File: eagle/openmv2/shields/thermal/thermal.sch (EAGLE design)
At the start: 10 parts, among them U1 MLX90620, U3 2.6v

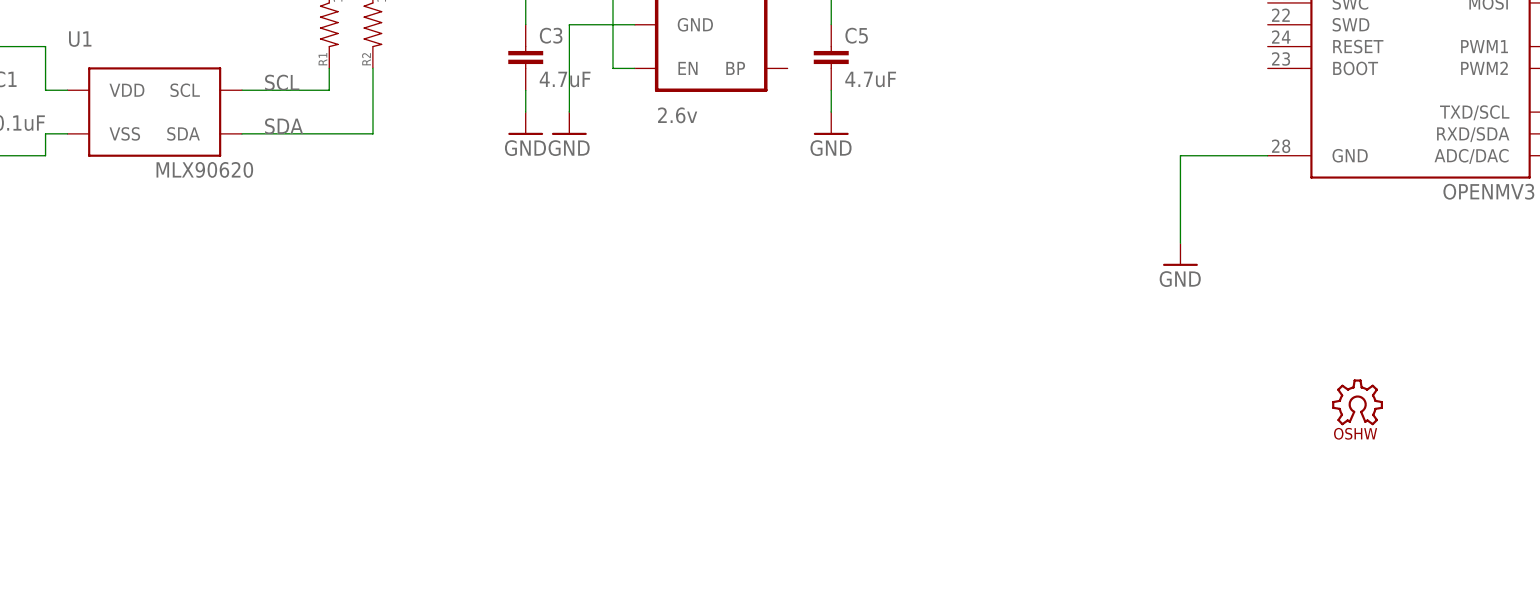
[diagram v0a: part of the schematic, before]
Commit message: Update shields silk-screen.
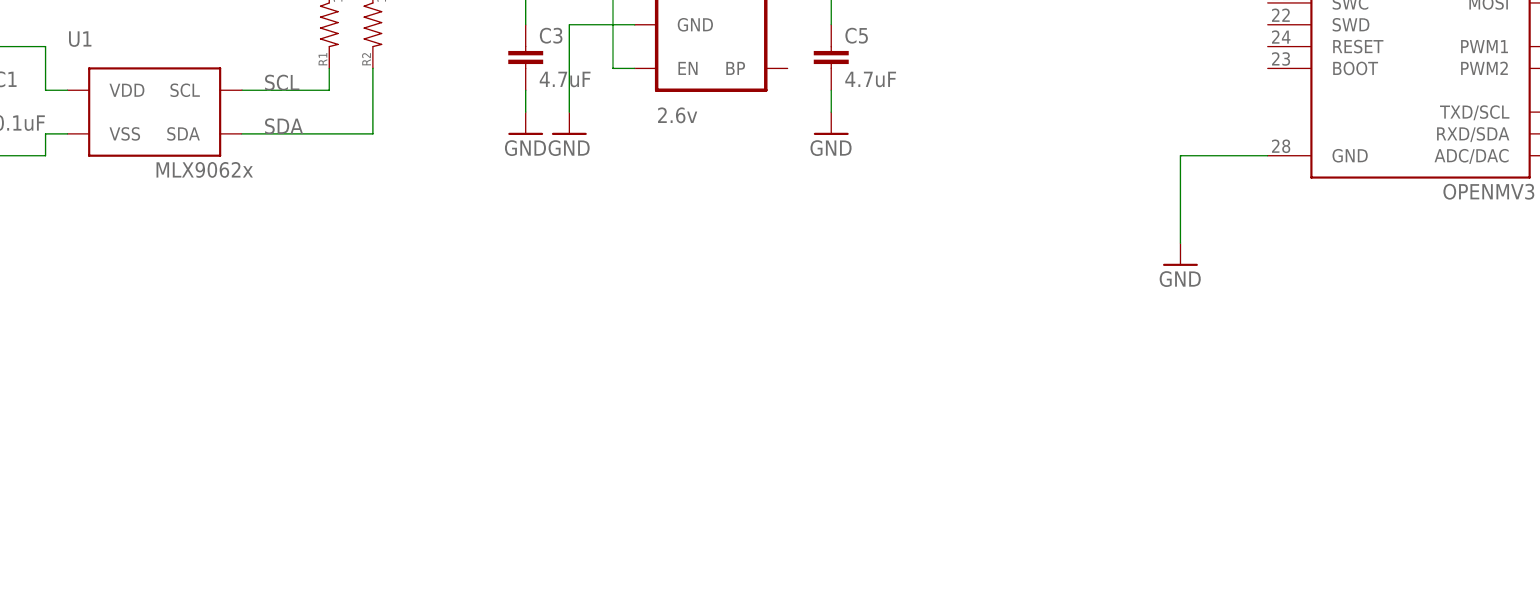
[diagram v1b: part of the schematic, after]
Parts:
- removed LOGO1: OSHW_LOGO_8MILX0150-NT, iofault:OSHW_LOGO_8MILX0150-NT
- U1: value MLX90620 -> MLX9062x
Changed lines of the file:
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@@
 <part name="GND4" library="supply1" deviceset="GND" device=""/>
 <part name="R2" library="sfe" deviceset="RESISTOR" device="0603-RES" value="10K"/>
-<part name="U1" library="MLX90620" deviceset="MLX90620" device=""/>
+<part name="U1" library="MLX90620" deviceset="MLX90620" device="" value="MLX9062x"/>
 <part name="C1" library="sfe" deviceset="CAP" device="0603-CAP" value="0.1uF"/>
 <part name="C2" library="sfe" deviceset="CAP" device="0603-CAP" value="0.01uF"/>
@@
 <part name="P+6" library="sfe" deviceset="3.3V" device=""/>
 <part name="P+7" library="sfe" deviceset="3.3V" device=""/>
-<part name="LOGO1" library="iofault" deviceset="OSHW_LOGO_8MIL" device="X0150-NT"/>
 </parts>
 <sheets>
@@
 <instance part="P+6" gate="G$1" x="88.9" y="86.36"/>
 <instance part="P+7" gate="G$1" x="111.76" y="88.9"/>
-<instance part="LOGO1" gate="G$1" x="205.74" y="27.94"/>
 </instances>
 <busses>
